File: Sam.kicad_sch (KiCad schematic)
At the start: 13 parts, among them IC1 MC6809E, J1 DataBus, J10 RGBS Interface, J2 Video, J3 AddressBus, J4 ControlOut, J5 ControlIn, J6 Video_In, J7 BusService, J9 Video_Out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

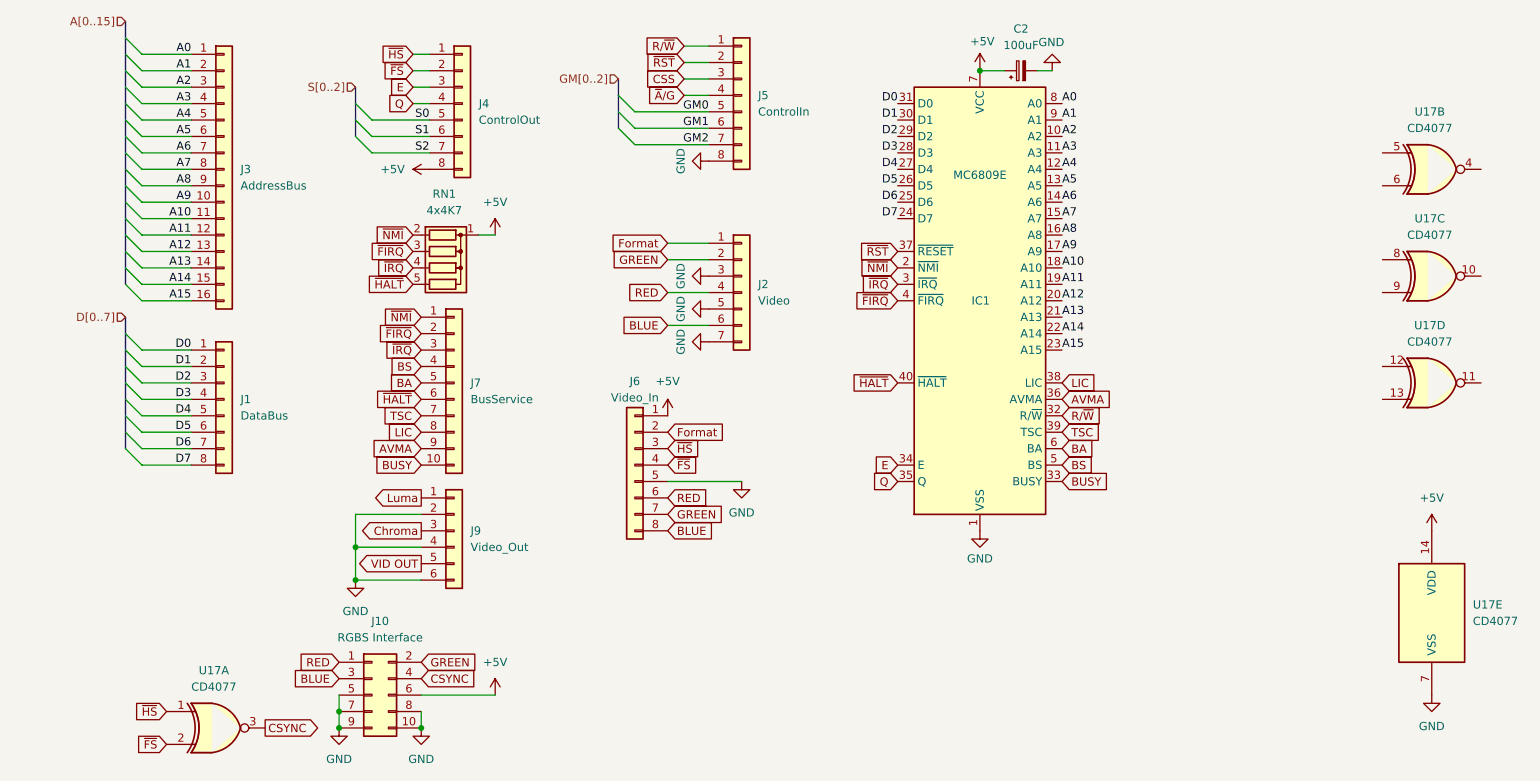
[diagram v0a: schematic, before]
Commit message: add audio support
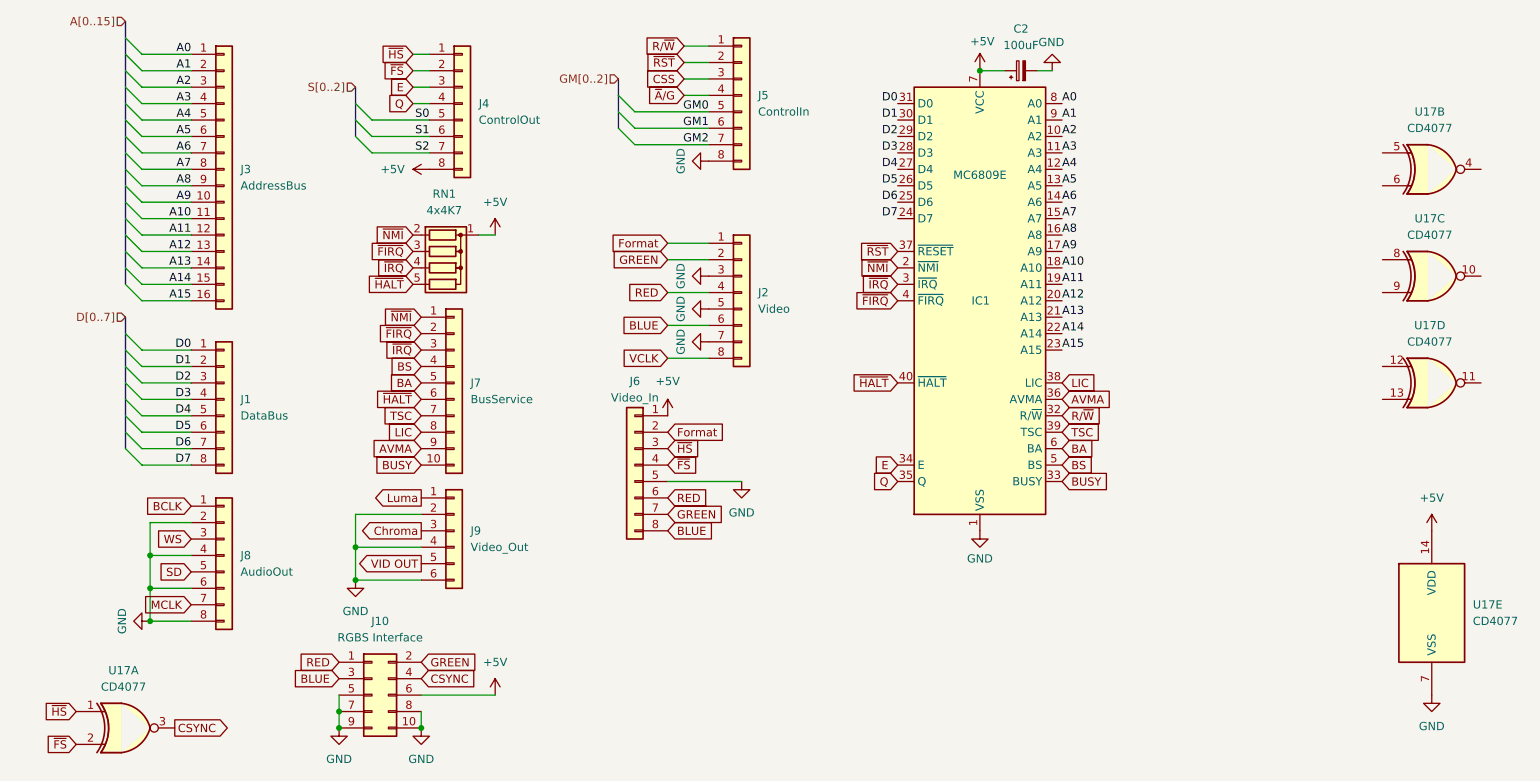
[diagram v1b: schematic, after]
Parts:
- added J8: AudioOut, Connector_PinHeader_2.54mm:PinHeader_1x08_P2.54mm_Vertical, symbol Connector_Generic:Conn_01x08
- J2: footprint Connector_PinHeader_2.54mm:PinHeader_1x07_P2.54mm_Vertical -> Connector_PinHeader_2.54mm:PinHeader_1x08_P2.54mm_Vertical; symbol Connector_Generic:Conn_01x07 -> Connector_Generic:Conn_01x08
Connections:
- net GND: now also J8.2 (Pin_2), J8.4 (Pin_4), J8.6 (Pin_6), J8.8 (Pin_8)
- new net BCLK: J8.1 (Pin_1)
- new net MCLK: J8.7 (Pin_7)
- new net SD: J8.5 (Pin_5)
- new net VCLK: J2.8 (Pin_8)
- new net WS: J8.3 (Pin_3)
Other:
- moved on the sheet: U17A
